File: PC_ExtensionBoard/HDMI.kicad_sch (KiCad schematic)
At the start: 41 parts, among them J1 Conn_01x26_MountingPin, Q10 2SK3018, Q11 2N7002, Q6 2SK3018, Q9 2SK3018, U5 TPAZ1023-04F, U6 TPAZ1023-04F

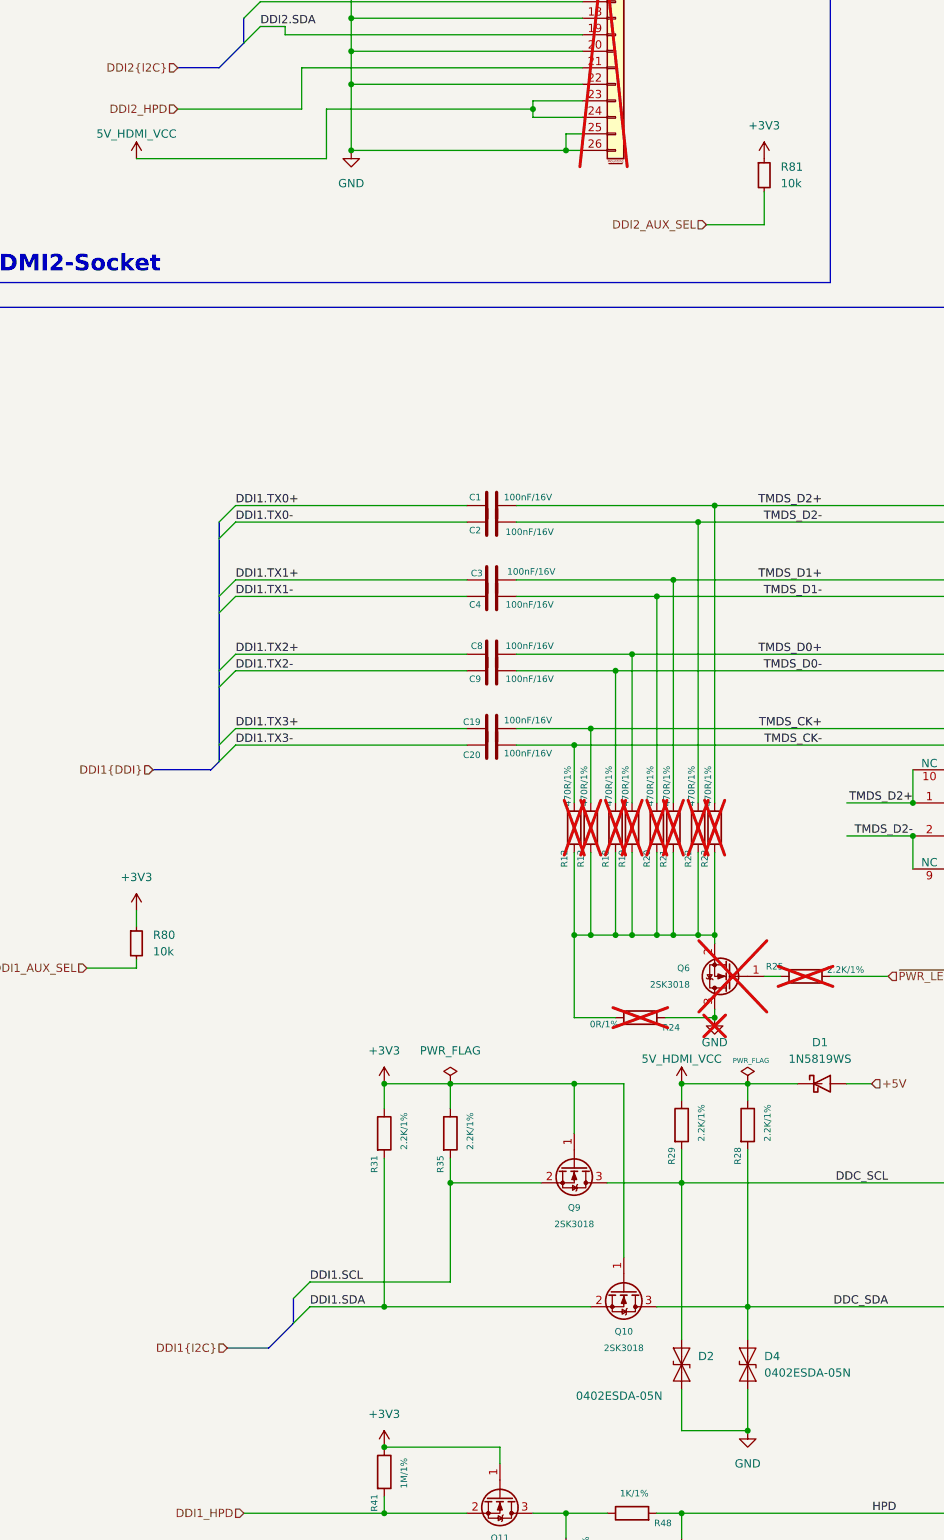
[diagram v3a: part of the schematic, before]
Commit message: attempts with impedance control
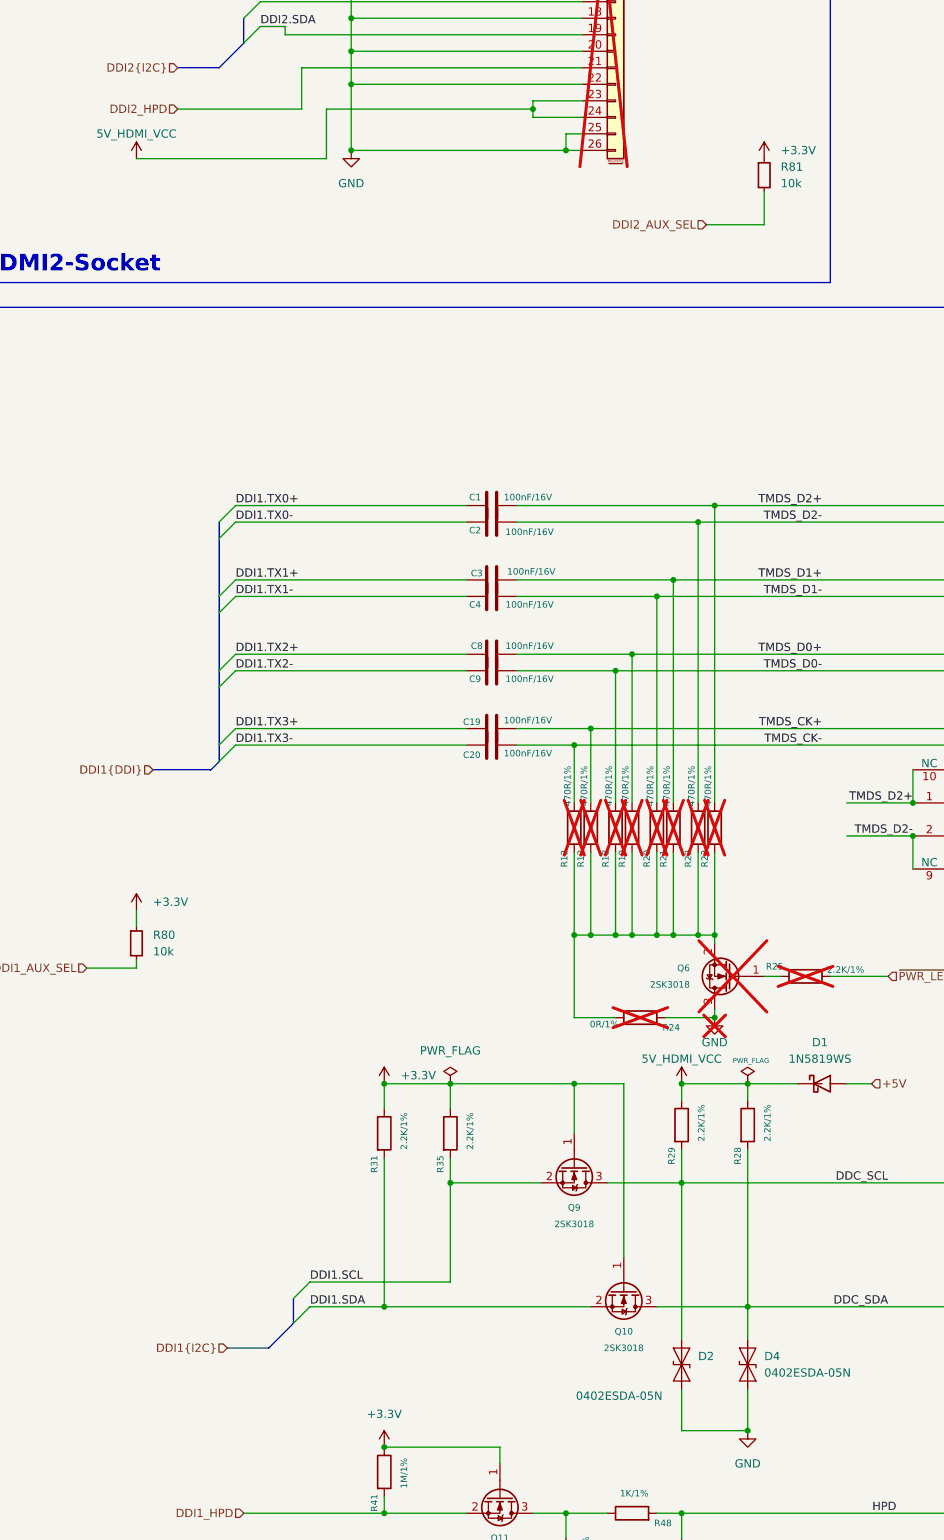
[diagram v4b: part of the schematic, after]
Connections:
- net +3V3 renamed +3.3V
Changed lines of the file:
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@@
 			)
 		)
-		(property "Value" "+3V3"
-			(at 81.28 307.34 0)
+		(property "Value" "+3.3V"
+			(at 83.82 311.1499 0)
 			(show_name no)
 			(do_not_autoplace no)
@@
 					(size 1.27 1.27)
 				)
+				(justify left)
 			)
 		)
@@
 			)
 		)
-		(property "Value" "+3V3"
-			(at 43.18 280.67 0)
+		(property "Value" "+3.3V"
+			(at 45.72 284.4799 0)
 			(show_name no)
 			(do_not_autoplace no)
@@
 					(size 1.27 1.27)
 				)
+				(justify left)
 			)
 		)
@@
 			)
 		)
-		(property "Value" "+3V3"
+		(property "Value" "+3.3V"
 			(at 81.28 363.22 0)
 			(show_name no)
@@
 			)
 		)
-		(property "Value" "+3V3"
-			(at 139.7 165.1 0)
+		(property "Value" "+3.3V"
+			(at 142.24 168.9099 0)
 			(show_name no)
 			(do_not_autoplace no)
@@
 					(size 1.27 1.27)
 				)
+				(justify left)
 			)
 		)
